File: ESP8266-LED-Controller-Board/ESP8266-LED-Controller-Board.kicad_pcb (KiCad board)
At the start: 2 copper layers, 70 x 38 mm, 49 parts, among them J1 Barrel_Jack_Switch, J2 USB_C_Receptacle_USB2.0, J3 Conn_01x04_Male, J4 Conn_01x05_Male, J5 Screw_Terminal_01x04, J6 Screw_Terminal_01x02, Q1 NTD5867NLT4G, Q2 NTD5867NLT4G, Q3 NTD5867NLT4G, Q4 NTD5867NLT4G, Q5 NTD5867NLT4G, SW1 SW_Push, SW2 SW_Push, U1 TPS563200, U2 ACS70331EESATR-005U3, U3 ESP-12F, U4 74LVC2G17DBVR

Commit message: Cleanup and exported STEP.
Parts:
- F1: footprint Fuse:Fuse_1206_3216Metric_Pad1.42x1.75mm_HandSolder -> Custom_components:Fuse_0ZCJ_1206
- turned F1 to 0 degrees
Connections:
- F1 pad 1: Net-(C1-Pad1) -> VDD
- F1 pad 2: VDD -> Net-(C1-Pad1)
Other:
- board text added: "5V to 12V"

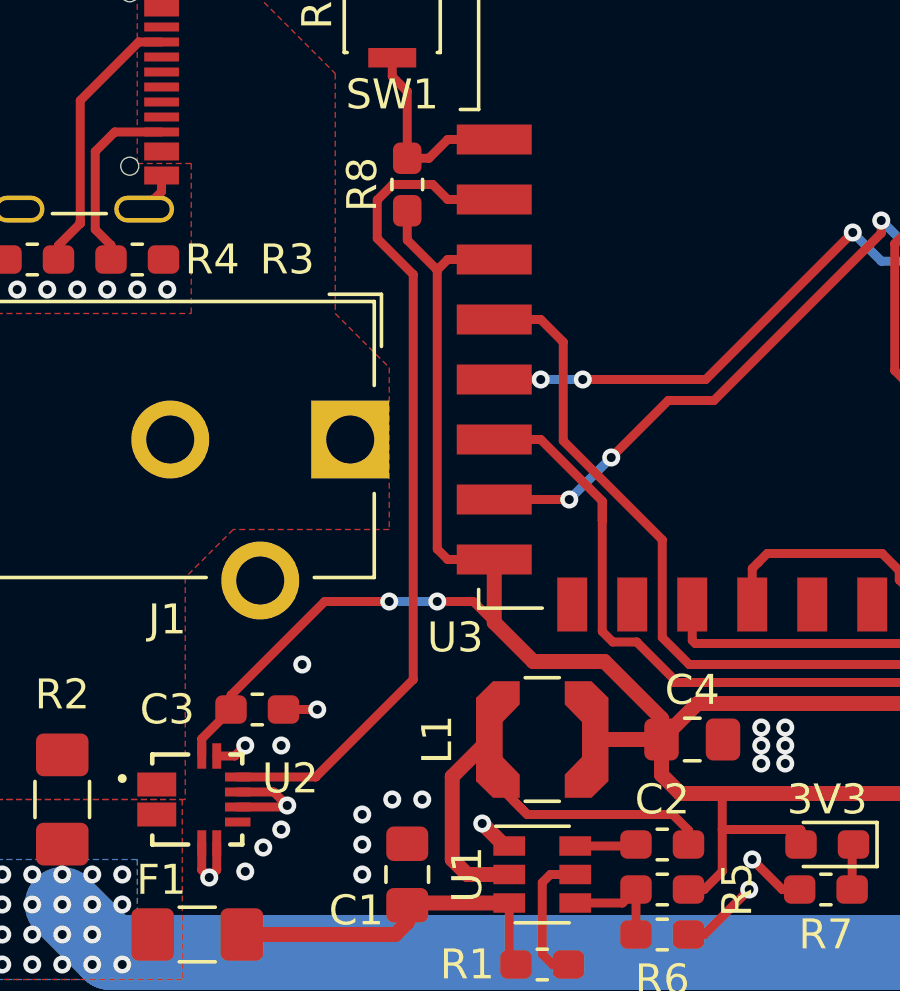
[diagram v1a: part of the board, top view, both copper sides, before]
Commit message: Added missing voltage divider for adc.
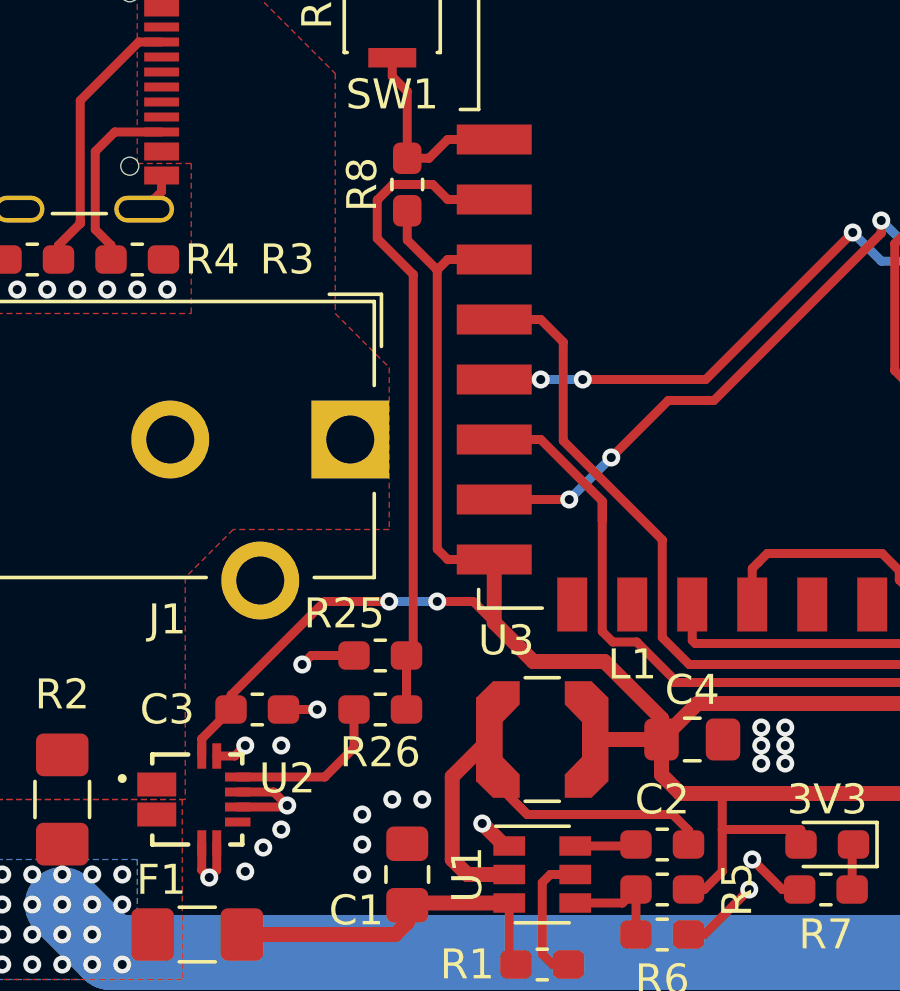
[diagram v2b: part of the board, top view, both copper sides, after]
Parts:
- added R25: 10k, Resistor_SMD:R_0603_1608Metric_Pad1.05x0.95mm_HandSolder, F.Cu at (114.1, 76.2)
- added R26: 22k, Resistor_SMD:R_0603_1608Metric_Pad1.05x0.95mm_HandSolder, F.Cu at (114.1, 78.0)
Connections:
- U3 pad 2: /I_MEASURE -> Net-(R25-Pad1)
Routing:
- net /I_MEASURE: track 28.0 -> 5.55 mm
- net Net-(R25-Pad1): track 0.00 -> 21.9 mm
- net GND: track 25.3 -> 27.1 mm
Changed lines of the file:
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@@
     (thickness 1.6)
     (drawings 49)
-    (tracks 581)
+    (tracks 587)
     (zones 0)
-    (modules 49)
-    (nets 40)
+    (modules 51)
+    (nets 41)
   )
   (page A4)
@@
   )
   (setup
-    (last_trace_width 0.25)
+    (last_trace_width 0.3)
     (user_trace_width 0.2)
     (user_trace_width 0.3)
@@
   (net 38 "Net-(R5-Pad2)")
   (net 39 "Net-(3V3-Pad1)")
+  (net 40 "Net-(R25-Pad1)")
   (net_class Default "This is the default net class."
     (clearance 0.2)
@@
     (add_net "Net-(Q5-Pad1)")
     (add_net "Net-(R1-Pad1)")
+    (add_net "Net-(R25-Pad1)")
     (add_net "Net-(R5-Pad2)")
+    (add_net "Net-(U3-Pad10)")
+    (add_net "Net-(U3-Pad13)")
+    (add_net "Net-(U3-Pad14)")
+    (add_net "Net-(U3-Pad9)")
     (add_net VDD)
     (add_net VIN)
@@
   (module Custom_components:ALLEGRO_ACS70331EESATR-005U3 (layer F.Cu)
     (at 108 81)
-    (fp_text reference U2 (at 3.1 -0.7) (layer F.SilkS)
+    (fp_text reference U2 (at 3 -0.7) (layer F.SilkS)
       (effects (font (size 1.001772 1.001772) (thickness 0.15)))
     )
@@
       (scale (xyz 1 1 1))
       (rotate (xyz -90 0 0))
+    )
+  )
+  (module Resistor_SMD:R_0603_1608Metric_Pad1.05x0.95mm_HandSolder (layer F.Cu)
+    (at 114.1 78 180)
+    (descr "Resistor SMD 0603 (1608 Metric), square (rectangular) end terminal, IPC_7351 nominal with elongated pad for handsoldering. (Body size source: http://www.tortai-tech.com/upload/download/2011102023233369053.pdf), generated with kicad-footprint-generator")
+    (tags "resistor handsolder")
+    (attr smd)
+    (fp_text reference R26 (at 0 -1.43) (layer F.SilkS)
+      (effects (font (size 1 1) (thickness 0.15)))
+    )
+    (fp_text value 22k (at 0 1.43) (layer F.Fab)
+      (effects (font (size 1 1) (thickness 0.15)))
+    )
+    (fp_text user %R (at 0 0) (layer F.Fab)
+      (effects (font (size 0.4 0.4) (thickness 0.06)))
+    )
+    (fp_line (start 1.65 0.73) (end -1.65 0.73) (layer F.CrtYd) (width 0.05))
+    (fp_line (start 1.65 -0.73) (end 1.65 0.73) (layer F.CrtYd) (width 0.05))
+    (fp_line (start -1.65 -0.73) (end 1.65 -0.73) (layer F.CrtYd) (width 0.05))
+    (fp_line (start -1.65 0.73) (end -1.65 -0.73) (layer F.CrtYd) (width 0.05))
+    (fp_line (start -0.171267 0.51) (end 0.171267 0.51) (layer F.SilkS) (width 0.12))
+    (fp_line (start -0.171267 -0.51) (end 0.171267 -0.51) (layer F.SilkS) (width 0.12))
+    (fp_line (start 0.8 0.4) (end -0.8 0.4) (layer F.Fab) (width 0.1))
+    (fp_line (start 0.8 -0.4) (end 0.8 0.4) (layer F.Fab) (width 0.1))
+    (fp_line (start -0.8 -0.4) (end 0.8 -0.4) (layer F.Fab) (width 0.1))
+    (fp_line (start -0.8 0.4) (end -0.8 -0.4) (layer F.Fab) (width 0.1))
+    (pad 2 smd roundrect (at 0.875 0 180) (size 1.05 0.95) (layers F.Cu F.Paste F.Mask) (roundrect_rratio 0.25)
+      (net 21 /I_MEASURE))
+    (pad 1 smd roundrect (at -0.875 0 180) (size 1.05 0.95) (layers F.Cu F.Paste F.Mask) (roundrect_rratio 0.25)
+      (net 40 "Net-(R25-Pad1)"))
+    (model ${KISYS3DMOD}/Resistor_SMD.3dshapes/R_0603_1608Metric.wrl
+      (at (xyz 0 0 0))
+      (scale (xyz 1 1 1))
+      (rotate (xyz 0 0 0))
+    )
+  )
+  (module Resistor_SMD:R_0603_1608Metric_Pad1.05x0.95mm_HandSolder (layer F.Cu)
+    (at 114.1 76.2 180)
+    (descr "Resistor SMD 0603 (1608 Metric), square (rectangular) end terminal, IPC_7351 nominal with elongated pad for handsoldering. (Body size source: http://www.tortai-tech.com/upload/download/2011102023233369053.pdf), generated with kicad-footprint-generator")
+    (tags "resistor handsolder")
+    (attr smd)
+    (fp_text reference R25 (at 1.2 1.4) (layer F.SilkS)
+      (effects (font (size 1 1) (thickness 0.15)))
+    )
+    (fp_text value 10k (at 0 1.43) (layer F.Fab)
+      (effects (font (size 1 1) (thickness 0.15)))
+    )
+    (fp_text user %R (at 0 0) (layer F.Fab)
+      (effects (font (size 0.4 0.4) (thickness 0.06)))
+    )
+    (fp_line (start 1.65 0.73) (end -1.65 0.73) (layer F.CrtYd) (width 0.05))
+    (fp_line (start 1.65 -0.73) (end 1.65 0.73) (layer F.CrtYd) (width 0.05))
+    (fp_line (start -1.65 -0.73) (end 1.65 -0.73) (layer F.CrtYd) (width 0.05))
+    (fp_line (start -1.65 0.73) (end -1.65 -0.73) (layer F.CrtYd) (width 0.05))
+    (fp_line (start -0.171267 0.51) (end 0.171267 0.51) (layer F.SilkS) (width 0.12))
+    (fp_line (start -0.171267 -0.51) (end 0.171267 -0.51) (layer F.SilkS) (width 0.12))
+    (fp_line (start 0.8 0.4) (end -0.8 0.4) (layer F.Fab) (width 0.1))
+    (fp_line (start 0.8 -0.4) (end 0.8 0.4) (layer F.Fab) (width 0.1))
+    (fp_line (start -0.8 -0.4) (end 0.8 -0.4) (layer F.Fab) (width 0.1))
+    (fp_line (start -0.8 0.4) (end -0.8 -0.4) (layer F.Fab) (width 0.1))
+    (pad 2 smd roundrect (at 0.875 0 180) (size 1.05 0.95) (layers F.Cu F.Paste F.Mask) (roundrect_rratio 0.25)
+      (net 6 GND))
+    (pad 1 smd roundrect (at -0.875 0 180) (size 1.05 0.95) (layers F.Cu F.Paste F.Mask) (roundrect_rratio 0.25)
+      (net 40 "Net-(R25-Pad1)"))
+    (model ${KISYS3DMOD}/Resistor_SMD.3dshapes/R_0603_1608Metric.wrl
+      (at (xyz 0 0 0))
+      (scale (xyz 1 1 1))
+      (rotate (xyz 0 0 0))
     )
   )
@@
     (tags "Wi-Fi Module")
     (attr smd)
-    (fp_text reference U3 (at -8.9 13.1 180) (layer F.SilkS)
+    (fp_text reference U3 (at -7.2 13.2 180) (layer F.SilkS)
       (effects (font (size 1 1) (thickness 0.15)))
     )
@@
       (net 7 +3V3))
     (pad 2 smd rect (at -7.6 -1.5) (size 2.5 1) (layers F.Cu F.Paste F.Mask)
-      (net 21 /I_MEASURE))
+      (net 40 "Net-(R25-Pad1)"))
     (pad 1 smd rect (at -7.6 -3.5) (size 2.5 1) (layers F.Cu F.Paste F.Mask)
       (net 32 /~RST~))
@@
     (tags "L Coilcraft LPS4012")
     (attr smd)
-    (fp_text reference L1 (at -3.5 0 90) (layer F.SilkS)
+    (fp_text reference L1 (at 3 -2.5 180) (layer F.SilkS)
       (effects (font (size 1 1) (thickness 0.15)))
     )
@@
   (via (at 102 51.5) (size 0.6) (drill 0.3) (layers F.Cu B.Cu) (net 6))
   (via (at 101 51.5) (size 0.6) (drill 0.3) (layers F.Cu B.Cu) (net 6))
+  (segment (start 111.8 76.2) (end 111.5 76.5) (width 0.3) (layer F.Cu) (net 6))
+  (segment (start 113.225 76.2) (end 111.8 76.2) (width 0.3) (layer F.Cu) (net 6))
   (segment (start 125.5 83.4) (end 125.5 82) (width 0.3) (layer F.Cu) (net 7))
   (segment (start 124.9 84) (end 125.5 83.4) (width 0.3) (layer F.Cu) (net 7))
@@
   (segment (start 124.95 67) (end 129.85 62.1) (width 0.3) (layer F.Cu) (net 20))
   (segment (start 120.85 67) (end 124.95 67) (width 0.3) (layer F.Cu) (net 20))
-  (segment (start 111.95 80.25) (end 109.35 80.25) (width 0.3) (layer F.Cu) (net 21))
-  (segment (start 115.2 77) (end 111.95 80.25) (width 0.3) (layer F.Cu) (net 21))
-  (segment (start 115.2 63.5) (end 115.2 77) (width 0.3) (layer F.Cu) (net 21))
-  (segment (start 114 62.3) (end 115.2 63.5) (width 0.3) (layer F.Cu) (net 21))
-  (segment (start 114.519134 60.5) (end 114 61.019134) (width 0.3) (layer F.Cu) (net 21))
-  (segment (start 115.85 60.5) (end 114.519134 60.5) (width 0.3) (layer F.Cu) (net 21))
-  (segment (start 116.35 61) (end 115.85 60.5) (width 0.3) (layer F.Cu) (net 21))
-  (segment (start 114 61.019134) (end 114 62.3) (width 0.3) (layer F.Cu) (net 21))
-  (segment (start 117.9 61) (end 116.35 61) (width 0.3) (layer F.Cu) (net 21))
+  (segment (start 109.35 80.25) (end 112.25 80.25) (width 0.3) (layer F.Cu) (net 21))
+  (segment (start 113.225 79.275) (end 113.225 78) (width 0.3) (layer F.Cu) (net 21))
+  (segment (start 112.25 80.25) (end 113.225 79.275) (width 0.3) (layer F.Cu) (net 21))
   (via (at 101.5 86.5) (size 0.6) (drill 0.3) (layers F.Cu B.Cu) (net 22))
   (via (at 102.5 86.5) (size 0.6) (drill 0.3) (layers F.Cu B.Cu) (net 22))
@@
   (segment (start 129.83 82.545) (end 129.875 82.5) (width 0.3) (layer F.Cu) (net 39))
   (segment (start 129.83 84) (end 129.83 82.545) (width 0.3) (layer F.Cu) (net 39))
+  (segment (start 114.975 78) (end 114.975 76.2) (width 0.3) (layer F.Cu) (net 40))
+  (segment (start 116.35 61) (end 117.9 61) (width 0.3) (layer F.Cu) (net 40))
+  (segment (start 114.519134 60.5) (end 115.85 60.5) (width 0.3) (layer F.Cu) (net 40))
+  (segment (start 114 61.019134) (end 114.519134 60.5) (width 0.3) (layer F.Cu) (net 40))
+  (segment (start 115 76.2) (end 115.2 76) (width 0.3) (layer F.Cu) (net 40))
+  (segment (start 115.2 63.5) (end 114 62.3) (width 0.3) (layer F.Cu) (net 40))
+  (segment (start 115.2 76) (end 115.2 63.5) (width 0.3) (layer F.Cu) (net 40))
+  (segment (start 115.85 60.5) (end 116.35 61) (width 0.3) (layer F.Cu) (net 40))
+  (segment (start 114 62.3) (end 114 61.019134) (width 0.3) (layer F.Cu) (net 40))
+  (segment (start 114.975 76.2) (end 115 76.2) (width 0.3) (layer F.Cu) (net 40))
   (zone (net 22) (net_name VDD) (layer F.Cu) (hatch edge 0.508)
     (priority 3)

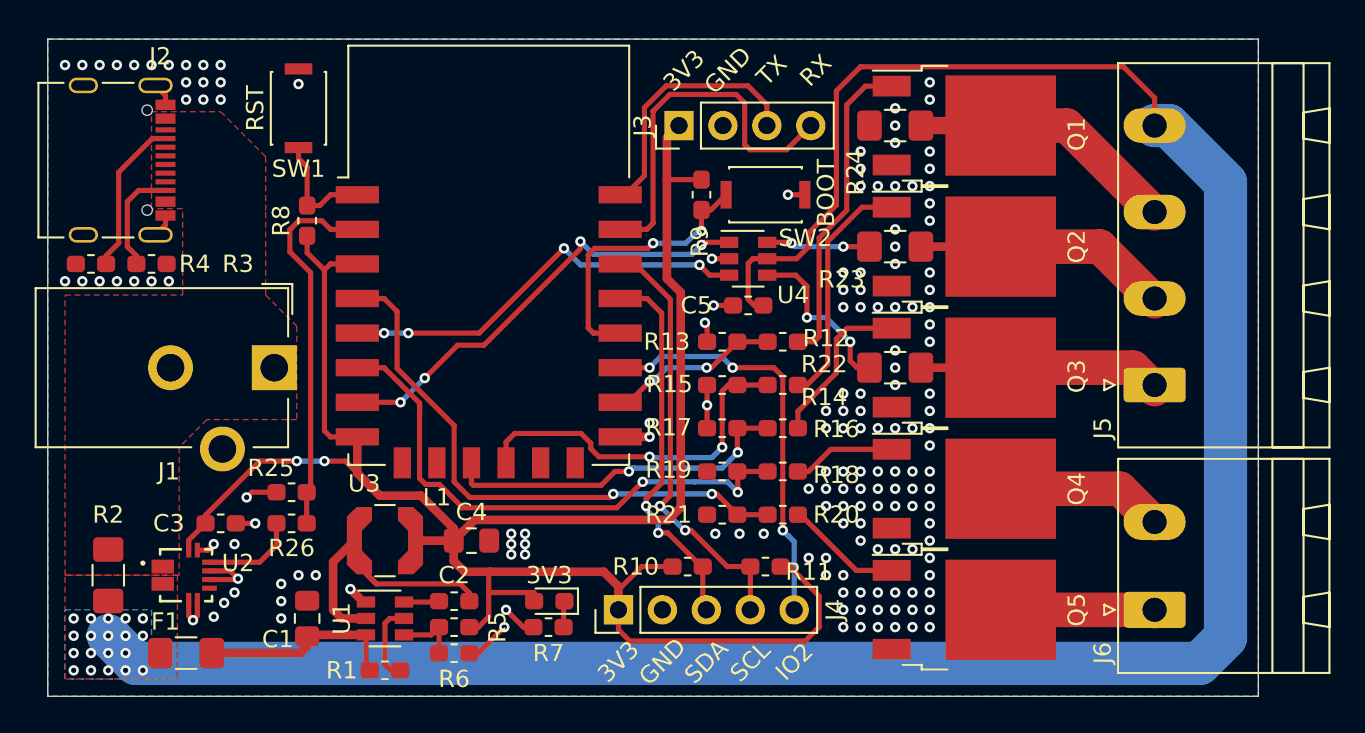
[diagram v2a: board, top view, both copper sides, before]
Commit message: Added pullup to EN pin just in case.
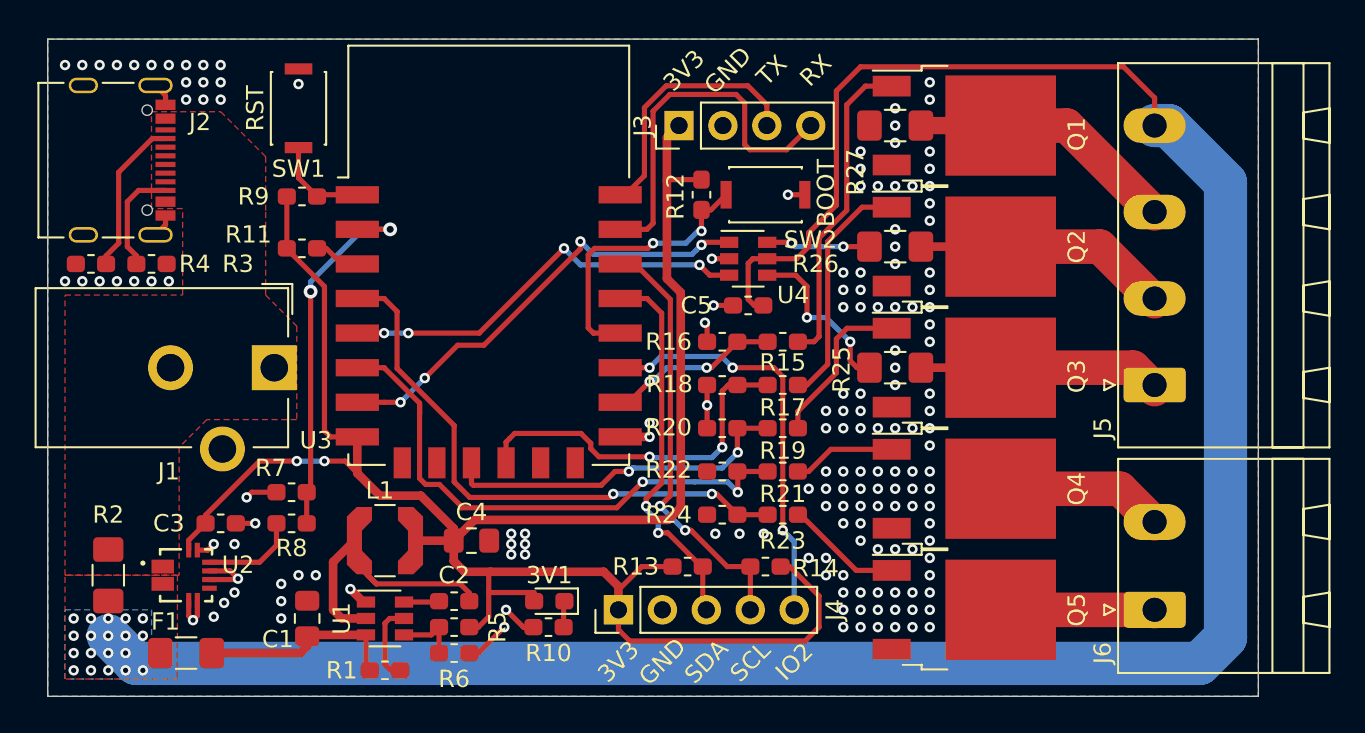
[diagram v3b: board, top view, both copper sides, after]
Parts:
- removed the R12 at (142.5, 67.5)
- added R11: 10k, Resistor_SMD:R_0603_1608Metric_Pad1.05x0.95mm_HandSolder, F.Cu at (114.7, 62.1)
- added R15: 100R, Resistor_SMD:R_0603_1608Metric_Pad1.05x0.95mm_HandSolder, F.Cu at (142.5, 67.5)
- moved R9 1.43 mm to (114.7, 59.1), turned to 0 degrees
- renumbered 3V3 to 3V1, R7 to R10, R9 to R12, R10 to R13, R11 to R14, R13 to R16, R14 to R17, R15 to R18, R16 to R19, R17 to R20, R18 to R21, R19 to R22, R20 to R23, R21 to R24, R22 to R25, R23 to R26, R24 to R27, R25 to R7, R26 to R8, R8 to R9
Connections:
- U3 pad 3: +3V3 -> Net-(R11-Pad2)
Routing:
- net Net-(R11-Pad2): track 0.00 -> 2.70 mm
- net /~RST~: track 6.72 -> 5.64 mm
- net +3V3: track 122.0 -> 122.7 mm
- net Net-(R7-Pad1): track 21.9 -> 21.8 mm, vias 0 -> 2
